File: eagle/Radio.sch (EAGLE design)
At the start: 134 parts, among them J500 2060-402, J501 2060-402, J920 2060-402, J921 2060-402, Q210 32.768kHz, Q610 32.768kHz, Q900 BSS123, U100 LP38693, U200 MSP430G2553, U300 IRF7103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

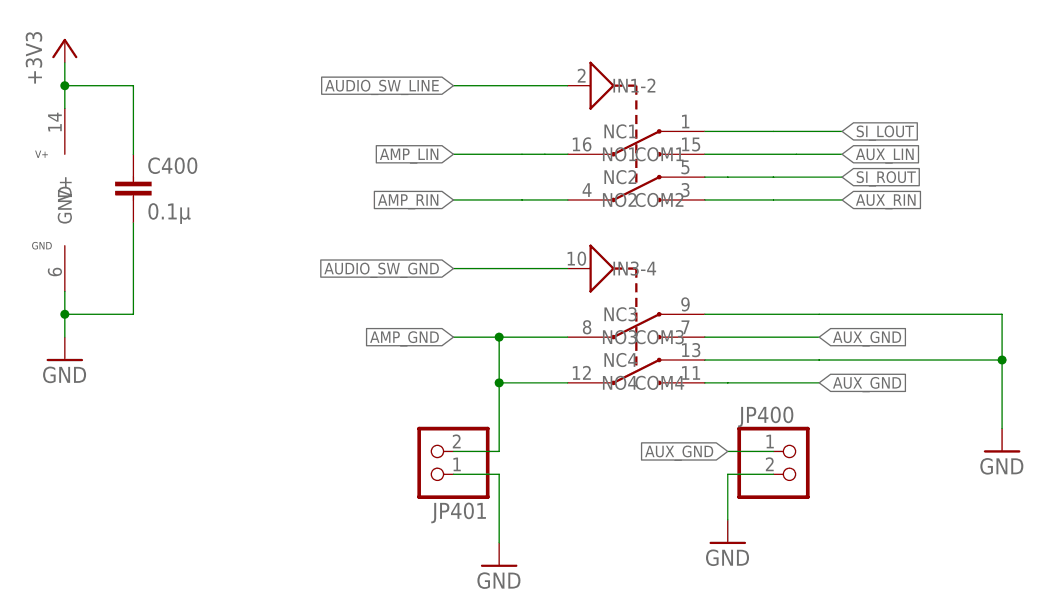
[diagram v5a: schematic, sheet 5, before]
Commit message: CHG: updated libary pathes for all non standart components to Radio Projekt.lbr
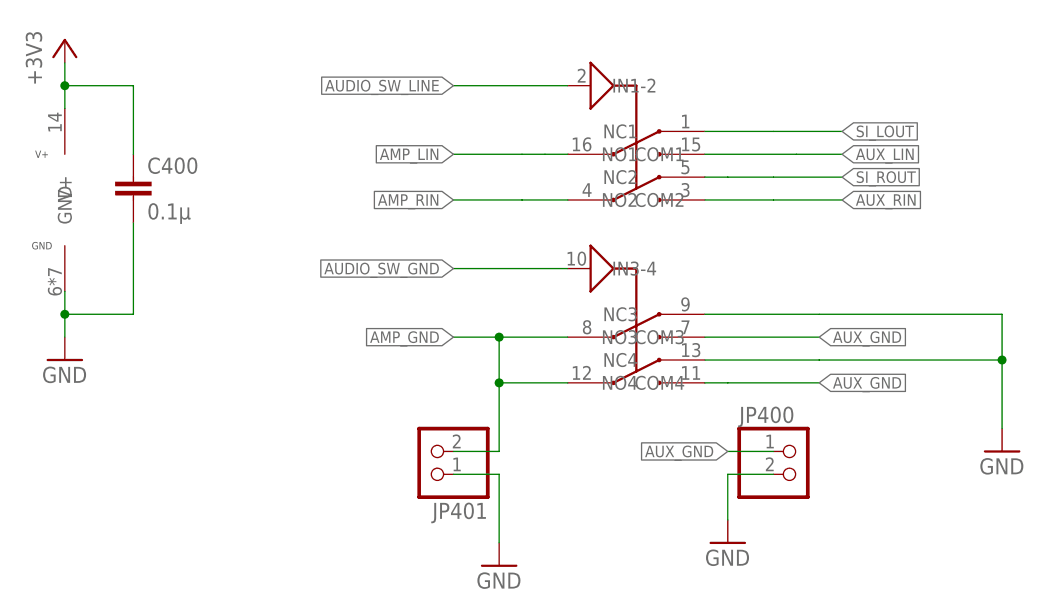
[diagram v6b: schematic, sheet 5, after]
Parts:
- J500, J501, J920, J921: device Wago-2060-402:2060-402 -> Radio Projekt:2060-402
- R602: value 10k -> DNB
- U400: device TI_Radio:TS3A44159RGT -> Radio Projekt:TS3A44159RGT
- U600: device SI473X-D60:SI473X-D60 -> Radio Projekt:SI473X-D60
- U920: device NXP_By_element14_Batch_1:PCA9632TK -> Radio Projekt:PCA9632TK
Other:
- moved on the sheet: U100, U200, U500, U600
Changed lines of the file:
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@@
 </classes>
 <parts>
-<part name="U600" library="SI473X-D60" deviceset="SI473X-D60" device=""/>
+<part name="U600" library="Radio Projekt" deviceset="SI473X-D60" device=""/>
 <part name="R601" library="rcl" deviceset="R-EU_" device="R1206" value="10k"/>
 <part name="C611" library="rcl" deviceset="C-EU" device="C1206K" value="22p"/>
@@
 <part name="GND8" library="supply1" deviceset="GND" device=""/>
 <part name="R600" library="rcl" deviceset="R-EU_" device="R1206" value="10k"/>
-<part name="R602" library="rcl" deviceset="R-EU_" device="R1206" value="10k"/>
+<part name="R602" library="rcl" deviceset="R-EU_" device="R1206" value="DNB"/>
 <part name="FRAME1" library="frames" deviceset="A4L-LOC" device="" value="SI4735"/>
 <part name="FRAME2" library="frames" deviceset="A4L-LOC" device="" value="TP2016D2"/>
@@
 <part name="U500" library="Radio Projekt" deviceset="TPA2016D2" device=""/>
 <part name="FRAME3" library="frames" deviceset="A5L-LOC" device="" value="Audio Switch"/>
-<part name="U400" library="TI_Radio" deviceset="TS3A44159" device="RGT"/>
+<part name="U400" library="Radio Projekt" deviceset="TS3A44159" device="RGT"/>
 <part name="X110" library="con-3m" deviceset="2510-" device="5"/>
 <part name="X100" library="con-3m" deviceset="2510-" device="5"/>
@@
 <part name="GND28" library="supply1" deviceset="GND" device=""/>
 <part name="R901" library="rcl" deviceset="R-EU_" device="R1206" value="1k"/>
-<part name="J501" library="Wago-2060-402" deviceset="2060-402" device=""/>
-<part name="J500" library="Wago-2060-402" deviceset="2060-402" device=""/>
-<part name="J921" library="Wago-2060-402" deviceset="2060-402" device=""/>
+<part name="J501" library="Radio Projekt" deviceset="2060-402" device=""/>
+<part name="J500" library="Radio Projekt" deviceset="2060-402" device=""/>
+<part name="J921" library="Radio Projekt" deviceset="2060-402" device=""/>
 <part name="P+4" library="supply1" deviceset="+5V" device=""/>
 <part name="JP400" library="pinhead" deviceset="PINHD-1X2" device=""/>
@@
 <part name="C940" library="rcl" deviceset="C-EU" device="C1206" value="0,1µ"/>
 <part name="GND38" library="supply1" deviceset="GND" device=""/>
-<part name="U920" library="NXP_By_element14_Batch_1" deviceset="PCA9632TK" device=""/>
+<part name="U920" library="Radio Projekt" deviceset="PCA9632TK" device=""/>
 <part name="GND39" library="supply1" deviceset="GND" device=""/>
-<part name="J920" library="Wago-2060-402" deviceset="2060-402" device=""/>
+<part name="J920" library="Radio Projekt" deviceset="2060-402" device=""/>
 <part name="U940" library="Radio Projekt" deviceset="OPT3001" device=""/>
 <part name="GND25" library="supply1" deviceset="GND" device=""/>

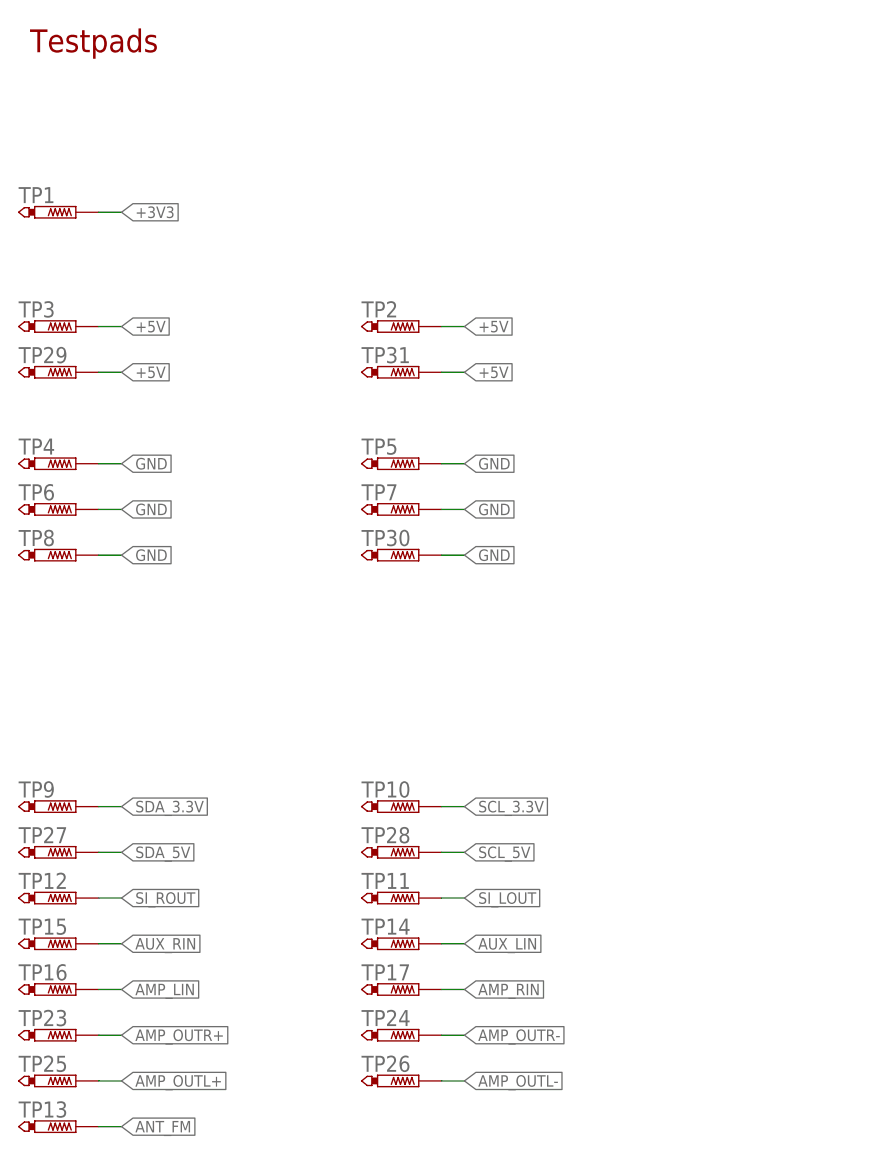
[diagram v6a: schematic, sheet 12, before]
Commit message: CHG: added some testpads for debugging methode
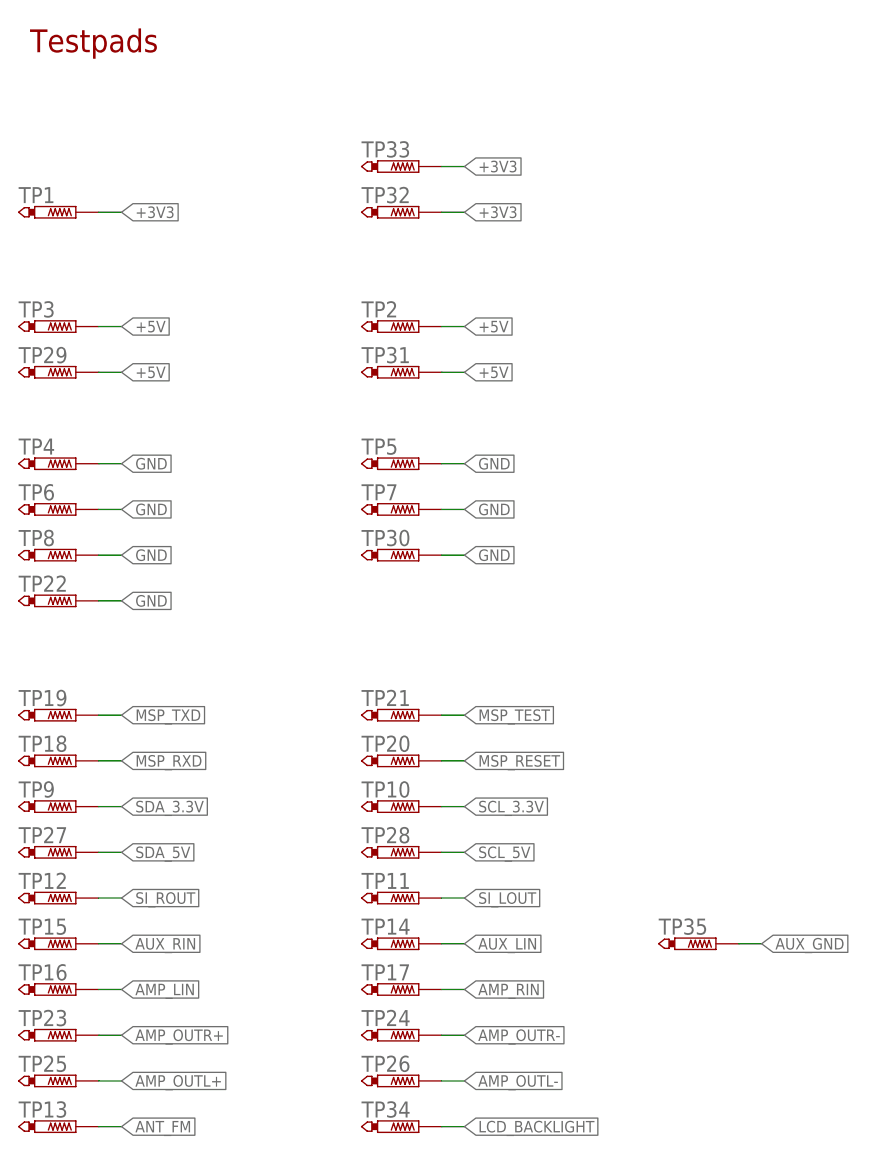
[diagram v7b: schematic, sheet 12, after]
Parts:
- added TP18, TP19, TP20, TP21, TP32, TP33, TP34, TP35: PTR1B1,27, testpad:PTR1B1,27
- added TP22: PTR1B2,54, testpad:PTR1B2,54
- C100, C110, C200, C400, C600, C652, C653, C654, C655, C901, C910, C920, L650: value 0.1µ -> 100n
- C500, C501, CP100, CP110: value 10µ -> 10u
- C800, C801, C802, C810, C811, C812: device rcl:C-EUC1206 -> rcl:C-EUC1206K
- C900, C903, C930, CP500, CP501, CP502, CP503: value 1µ -> 1u; device rcl:C-EUC1206 -> rcl:C-EUC1206K
- C940: value 0,1µ -> 100n; device rcl:C-EUC1206 -> rcl:C-EUC1206K
- D651, D652: value (none) -> 1N4148W
- L651: value 4.7µ -> 4u7
- L652: value 220µ -> 220u
- R900: value 4.7 -> 4R7
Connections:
- net +3V3: now also TP32.TP, TP33.TP
- net AUX_GND: now also TP35.TP
- net GND: now also TP22.TP
- net LCD_BACKLIGHT: now also TP34.TP
- net MSP_RESET: now also TP20.TP
- net MSP_RXD: now also TP18.TP
- net MSP_TEST: now also TP21.TP
- net MSP_TXD: now also TP19.TP
